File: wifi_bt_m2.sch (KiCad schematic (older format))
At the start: 24 parts, among them J1502 M.2_Key_E, Q1501 FDV301N, Q1502 FDV301N, SW1501 WWAN_HKS, U1502 74AUP2G00, U1504 NTB0104GU12, U1702 NTB0104GU12

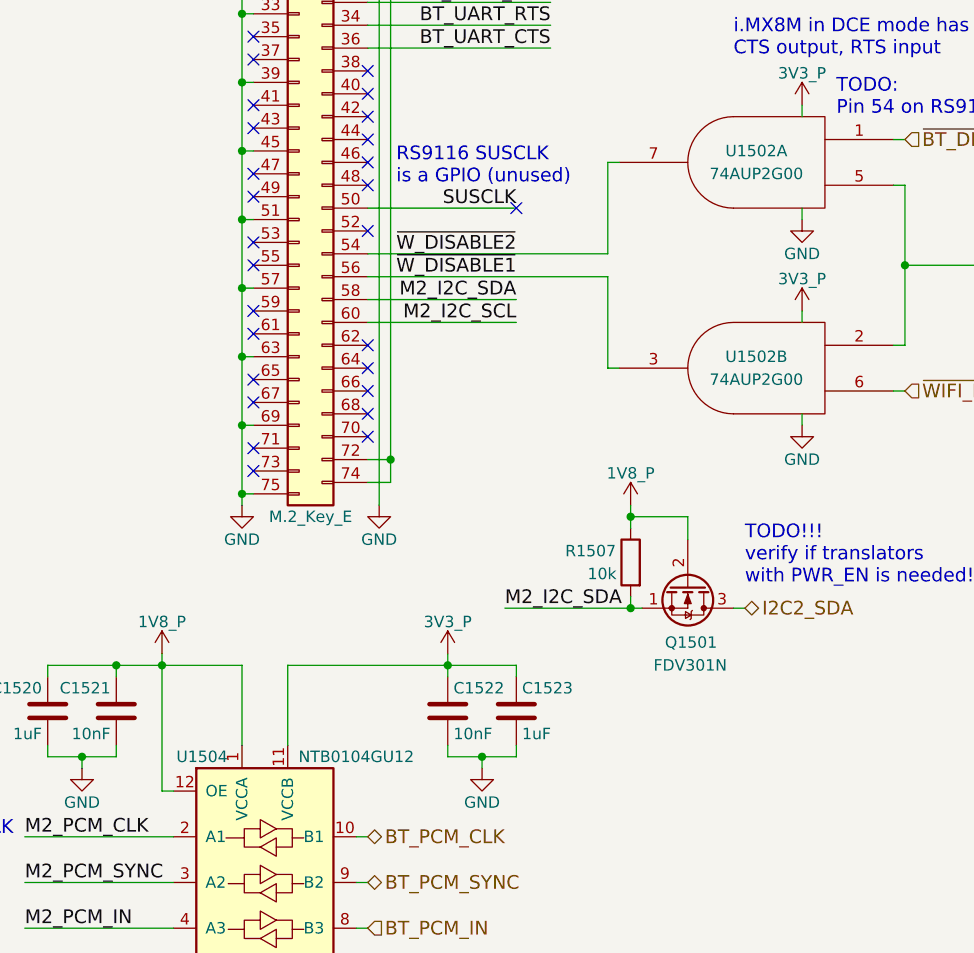
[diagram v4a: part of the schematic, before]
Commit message: Use SN74AUP2G08 instead of SN74AUP2G00 since the *08 is AND whereas the *00 is N AND
Since pin 54 is actually USB_VBUS sink on the RedPine module the baseboard may need to treat this pin specially (NXP EVK uses a NMOS inverter with a 10k pull-up to 3V3).
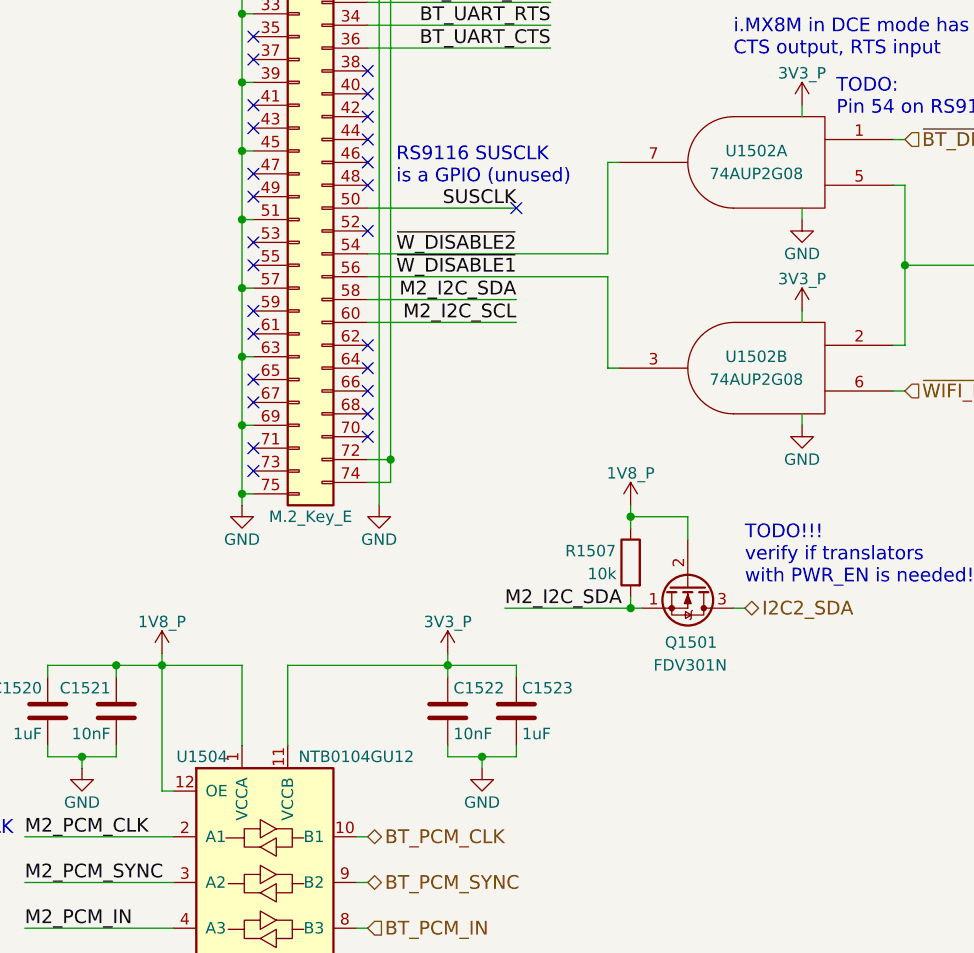
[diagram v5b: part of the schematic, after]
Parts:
- U1502: value 74AUP2G00 -> 74AUP2G08; Distrib Link https://www.digikey.com/product-detail/en/texas-instruments/SN74AUP2G00DCUR/296-36884-1-ND/4376315 -> https://www.digikey.com/product-detail/en/texas-instruments/SN74AUP2G08DCUR/296-32271-1-ND/3505517; Distrib PN 296-36884-1-ND -> 296-32271-1-ND; MFG Part Num SN74AUP2G00DCUR -> SN74AUP2G08DCUR; Others https://www.digikey.com/products/en/integrated-circuits-ics/logic-gates-and-inverters/705?quantity=&ColumnSort=1000011&page=1&k=74AUP2G00&pageSize=500 -> https://www.digikey.com/products/en/integrated-circuits-ics/logic-gates-and-inverters/705?k=74AUP2G08
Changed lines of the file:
@@
 P 7550 3550
 F 0 "U1502" H 7550 3600 50  0000 C CNN
-F 1 "74AUP2G00" H 7550 3500 50  0000 C CNN
+F 1 "74AUP2G08" H 7550 3500 50  0000 C CNN
 F 2 "" H 7550 3550 50  0001 C CNN
-F 3 "http://www.ti.com/lit/ds/symlink/sn74aup2g00.pdf" H 7550 3550 50  0001 C CNN
+F 3 "http://www.ti.com/lit/ds/symlink/sn74aup2g08.pdf" H 7550 3550 50  0001 C CNN
 F 4 "Texas Instruments" H 7550 3550 60  0001 C CNN "MFG Name"
-F 5 "SN74AUP2G00DCUR" H 7550 3550 60  0001 C CNN "MFG Part Num"
-F 6 "296-36884-1-ND" H 7550 3550 60  0001 C CNN "Distrib PN"
-F 7 "https://www.digikey.com/product-detail/en/texas-instruments/SN74AUP2G00DCUR/296-36884-1-ND/4376315" H 7550 3550 60  0001 C CNN "Distrib Link"
+F 5 "SN74AUP2G08DCUR" H 7550 3550 60  0001 C CNN "MFG Part Num"
+F 6 "296-32271-1-ND" H 7550 3550 60  0001 C CNN "Distrib PN"
+F 7 "https://www.digikey.com/product-detail/en/texas-instruments/SN74AUP2G08DCUR/296-32271-1-ND/3505517" H 7550 3550 60  0001 C CNN "Distrib Link"
 F 8 "-" H 7550 3550 60  0001 C CNN "Tolerance"
-F 9 "https://www.digikey.com/products/en/integrated-circuits-ics/logic-gates-and-inverters/705?quantity=&ColumnSort=1000011&page=1&k=74AUP2G00&pageSize=500" H 7550 3550 60  0001 C CNN "Others"
+F 9 "https://www.digikey.com/products/en/integrated-circuits-ics/logic-gates-and-inverters/705?k=74AUP2G08" H 7550 3550 60  0001 C CNN "Others"
 	1    7550 3550
 	-1   0    0    -1
@@
 	9650 5100 9400 5100
 Connection ~ 9400 5100
-$Comp
-L 74AUP2G00 U1502
-U 2 1 5AEC3CE9
-P 7550 4450
-F 0 "U1502" H 7550 4500 50  0000 C CNN
-F 1 "74AUP2G00" H 7550 4400 50  0000 C CNN
-F 2 "" H 7550 4450 50  0001 C CNN
-F 3 "http://www.ti.com/lit/ds/symlink/sn74aup2g00.pdf" H 7550 4450 50  0001 C CNN
-F 4 "Texas Instruments" H 7550 4450 60  0001 C CNN "MFG Name"
-F 5 "SN74AUP2G00DCUR" H 7550 4450 60  0001 C CNN "MFG Part Num"
-F 6 "296-36884-1-ND" H 7550 4450 60  0001 C CNN "Distrib PN"
-F 7 "https://www.digikey.com/product-detail/en/texas-instruments/SN74AUP2G00DCUR/296-36884-1-ND/4376315" H 7550 4450 60  0001 C CNN "Distrib Link"
-F 8 "-" H 7550 4450 60  0001 C CNN "Tolerance"
-F 9 "https://www.digikey.com/products/en/integrated-circuits-ics/logic-gates-and-inverters/705?quantity=&ColumnSort=1000011&page=1&k=74AUP2G00&pageSize=500" H 7550 4450 60  0001 C CNN "Others"
-	2    7550 4450
-	-1   0    0    -1
-$EndComp
 Text Notes 1150 7550 0    60   ~ 0
 internal 10k pull-up
@@
 	5400 7550 5400 7500
 Wire Wire Line
-	5000 6300 4950 6300
+	4950 6300 5000 6300
 Connection ~ 4950 5750
 Wire Wire Line
@@
 	5300 5750 5300 6100
 Wire Wire Line
-	4950 6300 4950 5700
+	4950 5700 4950 6300
 Wire Wire Line
 	1800 5700 1800 6300
@@
 Text Notes 2950 1250 0    60   ~ 0
 RS9116 datasheet says\nno WIFI_WAKE\nbut the schematic has it
+$Comp
+L 74AUP2G00 U1502
+U 2 1 5B14C873
+P 7550 4450
+F 0 "U1502" H 7550 4500 50  0000 C CNN
+F 1 "74AUP2G08" H 7550 4400 50  0000 C CNN
+F 2 "" H 7550 4450 50  0001 C CNN
+F 3 "http://www.ti.com/lit/ds/symlink/sn74aup2g08.pdf" H 7550 4450 50  0001 C CNN
+F 4 "Texas Instruments" H 7550 4450 60  0001 C CNN "MFG Name"
+F 5 "SN74AUP2G08DCUR" H 7550 4450 60  0001 C CNN "MFG Part Num"
+F 6 "296-32271-1-ND" H 7550 4450 60  0001 C CNN "Distrib PN"
+F 7 "https://www.digikey.com/product-detail/en/texas-instruments/SN74AUP2G08DCUR/296-32271-1-ND/3505517" H 7550 4450 60  0001 C CNN "Distrib Link"
+F 8 "-" H 7550 4450 60  0001 C CNN "Tolerance"
+F 9 "https://www.digikey.com/products/en/integrated-circuits-ics/logic-gates-and-inverters/705?k=74AUP2G08" H 7550 4450 60  0001 C CNN "Others"
+	2    7550 4450
+	-1   0    0    -1
+$EndComp
 $EndSCHEMATC

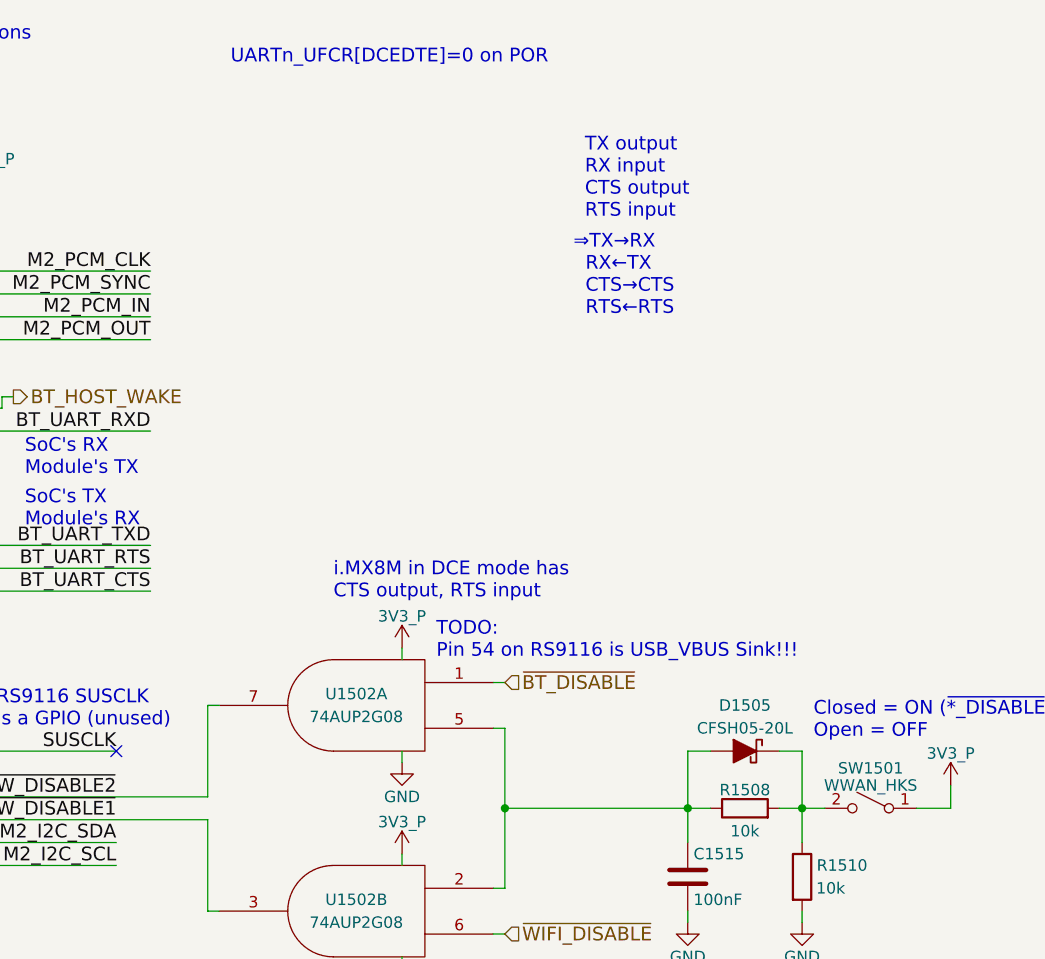
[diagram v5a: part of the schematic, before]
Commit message: Assign SAI5 to the WLAN/BT M.2, remove SIM2 slot due to conflicts between modules (specifically the L830-EB being a Config_0 module where the TX_BLANKING signal would connected to USIM_PWR2 sink), reassign the corresponding M.2 config pin to handle HP_DET, remove the AMOLED buck-boost as a different regulator will be used
The MIC_SEL, PROX_~INT, IMU_INT, and HAPTIC signals still need assigning
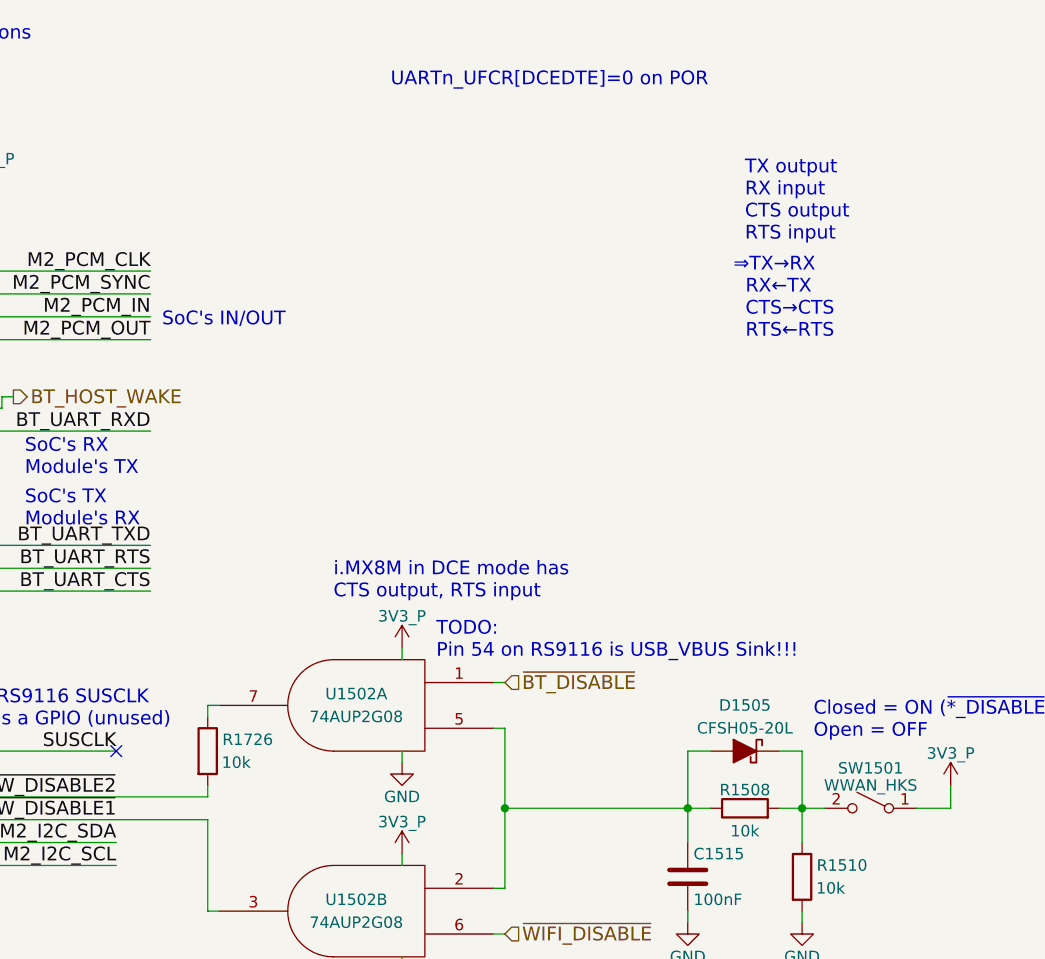
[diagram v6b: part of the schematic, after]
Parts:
- added R1726: 10k, symbol R
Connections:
- net ~W_DISABLE2: now also R1726.2; no longer U1502.7
- new net: R1726.1, U1502.7
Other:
- note added: "SoC's IN/OUT"
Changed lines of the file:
@@
 	5350 1500 5250 1500
 $Comp
-L GND #PWR0283
+L GND #PWR0256
 U 1 1 5B01D9F9
 P 5300 5050
-F 0 "#PWR0283" H 5300 4800 50  0001 C CNN
+F 0 "#PWR0256" H 5300 4800 50  0001 C CNN
 F 1 "GND" H 5300 4900 50  0000 C CNN
 F 2 "" H 5300 5050 50  0001 C CNN
@@
 Connection ~ 5300 5000
 $Comp
-L GND #PWR0284
+L GND #PWR0257
 U 1 1 5B01E5BE
 P 5900 5050
-F 0 "#PWR0284" H 5900 4800 50  0001 C CNN
+F 0 "#PWR0257" H 5900 4800 50  0001 C CNN
 F 1 "GND" H 5900 4900 50  0000 C CNN
 F 2 "" H 5900 5050 50  0001 C CNN
@@
 	5900 2150 5900 5050
 $Comp
-L 3V3_P #PWR0285
+L 3V3_P #PWR0258
 U 1 1 5B01E6B8
 P 5950 1300
-F 0 "#PWR0285" H 5950 1150 50  0001 C CNN
+F 0 "#PWR0258" H 5950 1150 50  0001 C CNN
 F 1 "3V3_P" H 5950 1440 50  0000 C CNN
 F 2 "" H 5950 1300 50  0001 C CNN
@@
 6.2 M.2 Signal Directions
 $Bitmap
-Pos 7850 1200
+Pos 8550 1300
 Scale 1.000000
 Data
@@
 EndData
 $EndBitmap
-Text Notes 8550 1425 0    60   ~ 0
+Text Notes 9250 1525 0    60   ~ 0
 TX output\nRX input\nCTS output\nRTS input
-Text Notes 8500 1850 0    60   ~ 0
+Text Notes 9200 1950 0    60   ~ 0
 ⇒TX→RX\n  RX←TX\n  CTS→CTS\n  RTS←RTS
 Text Notes 7450 3090 0    60   ~ 0
 i.MX8M in DCE mode has\nCTS output, RTS input
-Text Notes 7000 750  0    60   ~ 0
+Text Notes 7700 850  0    60   ~ 0
 UARTn_UFCR[DCEDTE]=0 on POR
 Wire Wire Line
@@
 $EndComp
 $Comp
-L 3V3_P #PWR0286
+L 3V3_P #PWR0259
 U 1 1 5B0C3C8A
 P 10150 3900
-F 0 "#PWR0286" H 10150 3750 50  0001 C CNN
+F 0 "#PWR0259" H 10150 3750 50  0001 C CNN
 F 1 "3V3_P" H 10150 4040 50  0000 C CNN
 F 2 "" H 10150 3900 50  0001 C CNN
@@
 Wire Wire Line
 	6900 4450 6950 4450
-Wire Wire Line
-	6900 3950 6900 3550
 Wire Wire Line
 	6900 3550 6950 3550
@@
 NoConn ~ 6500 3750
 $Comp
-L 3V3_P #PWR0287
+L 3V3_P #PWR0260
 U 1 1 5B0D90EE
 P 7750 3300
-F 0 "#PWR0287" H 7750 3150 50  0001 C CNN
+F 0 "#PWR0260" H 7750 3150 50  0001 C CNN
 F 1 "3V3_P" H 7750 3440 50  0000 C CNN
 F 2 "" H 7750 3300 50  0001 C CNN
@@
 	7750 3300 7750 3350
 $Comp
-L GND #PWR0288
+L GND #PWR0261
 U 1 1 5B0D91C5
 P 7750 4700
-F 0 "#PWR0288" H 7750 4450 50  0001 C CNN
+F 0 "#PWR0261" H 7750 4450 50  0001 C CNN
 F 1 "GND" H 7750 4550 50  0000 C CNN
 F 2 "" H 7750 4700 50  0001 C CNN
@@
 Connection ~ 4550 2400
 $Comp
-L 1V8_P #PWR0289
+L 1V8_P #PWR0262
 U 1 1 5AEFAF82
 P 4550 2000
-F 0 "#PWR0289" H 4550 1850 50  0001 C CNN
+F 0 "#PWR0262" H 4550 1850 50  0001 C CNN
 F 1 "1V8_P" H 4550 2140 50  0000 C CNN
 F 2 "" H 4550 2000 50  0001 C CNN
@@
 $EndComp
 $Comp
-L 1V8_P #PWR0290
+L 1V8_P #PWR0263
 U 1 1 5AEB9155
 P 7000 5050
-F 0 "#PWR0290" H 7000 4900 50  0001 C CNN
+F 0 "#PWR0263" H 7000 4900 50  0001 C CNN
 F 1 "1V8_P" H 7000 5190 50  0000 C CNN
 F 2 "" H 7000 5050 50  0001 C CNN
@@
 TODO!!!\nverify if translators\nwith PWR_EN is needed!
 $Comp
-L 3V3_P #PWR0291
+L 3V3_P #PWR0264
 U 1 1 5AF2CD0D
 P 7750 4200
-F 0 "#PWR0291" H 7750 4050 50  0001 C CNN
+F 0 "#PWR0264" H 7750 4050 50  0001 C CNN
 F 1 "3V3_P" H 7750 4340 50  0000 C CNN
 F 2 "" H 7750 4200 50  0001 C CNN
@@
 	7750 4200 7750 4250
 $Comp
-L GND #PWR0292
+L GND #PWR0265
 U 1 1 5AF2CDB4
 P 7750 3800
-F 0 "#PWR0292" H 7750 3550 50  0001 C CNN
+F 0 "#PWR0265" H 7750 3550 50  0001 C CNN
 F 1 "GND" H 7750 3650 50  0000 C CNN
 F 2 "" H 7750 3800 50  0001 C CNN
@@
 $EndComp
 $Comp
-L GND #PWR0293
+L GND #PWR0266
 U 1 1 5AF3C984
 P 9000 4500
-F 0 "#PWR0293" H 9000 4250 50  0001 C CNN
+F 0 "#PWR0266" H 9000 4250 50  0001 C CNN
 F 1 "GND" H 9000 4350 50  0000 C CNN
 F 2 "" H 9000 4500 50  0001 C CNN
@@
 $EndComp
 $Comp
-L GND #PWR0294
+L GND #PWR0267
 U 1 1 5AF3C98A
 P 9500 4500
-F 0 "#PWR0294" H 9500 4250 50  0001 C CNN
+F 0 "#PWR0267" H 9500 4250 50  0001 C CNN
 F 1 "GND" H 9500 4350 50  0000 C CNN
 F 2 "" H 9500 4500 50  0001 C CNN
@@
 $EndComp
 $Comp
-L 1V8_P #PWR0295
+L 1V8_P #PWR0268
 U 1 1 5AEBC081
 P 9400 5050
-F 0 "#PWR0295" H 9400 4900 50  0001 C CNN
+F 0 "#PWR0268" H 9400 4900 50  0001 C CNN
 F 1 "1V8_P" H 9400 5190 50  0000 C CNN
 F 2 "" H 9400 5050 50  0001 C CNN
@@
 $EndComp
 $Comp
-L GND #PWR0296
+L GND #PWR0269
 U 1 1 5B2489BD
 P 6350 6200
-F 0 "#PWR0296" H 6350 5950 50  0001 C CNN
+F 0 "#PWR0269" H 6350 5950 50  0001 C CNN
 F 1 "GND" H 6350 6050 50  0000 C CNN
 F 2 "" H 6350 6200 50  0001 C CNN
@@
 $EndComp
 $Comp
-L GND #PWR0297
+L GND #PWR0270
 U 1 1 5B2489DB
 P 4600 6200
-F 0 "#PWR0297" H 4600 5950 50  0001 C CNN
+F 0 "#PWR0270" H 4600 5950 50  0001 C CNN
 F 1 "GND" H 4600 6050 50  0000 C CNN
 F 2 "" H 4600 6200 50  0001 C CNN
@@
 	4450 5750 5300 5750
 $Comp
-L GND #PWR0298
+L GND #PWR0271
 U 1 1 5B2489F2
 P 5400 7550
-F 0 "#PWR0298" H 5400 7300 50  0001 C CNN
+F 0 "#PWR0271" H 5400 7300 50  0001 C CNN
 F 1 "GND" H 5400 7400 50  0000 C CNN
 F 2 "" H 5400 7550 50  0001 C CNN
@@
 BCLK
 $Comp
-L 3V3_P #PWR0299
+L 3V3_P #PWR0272
 U 1 1 5B248A11
 P 6200 5700
-F 0 "#PWR0299" H 6200 5550 50  0001 C CNN
+F 0 "#PWR0272" H 6200 5550 50  0001 C CNN
 F 1 "3V3_P" H 6200 5840 50  0000 C CNN
 F 2 "" H 6200 5700 50  0001 C CNN
@@
 $EndComp
 $Comp
-L 1V8_P #PWR0300
+L 1V8_P #PWR0273
 U 1 1 5B248A1D
 P 4950 5700
-F 0 "#PWR0300" H 4950 5550 50  0001 C CNN
+F 0 "#PWR0273" H 4950 5550 50  0001 C CNN
 F 1 "1V8_P" H 4950 5840 50  0000 C CNN
 F 2 "" H 4950 5700 50  0001 C CNN
@@
 $EndComp
 $Comp
-L GND #PWR0301
+L GND #PWR0274
 U 1 1 5B337EDE
 P 3200 6200
-F 0 "#PWR0301" H 3200 5950 50  0001 C CNN
+F 0 "#PWR0274" H 3200 5950 50  0001 C CNN
 F 1 "GND" H 3200 6050 50  0000 C CNN
 F 2 "" H 3200 6200 50  0001 C CNN
@@
 $EndComp
 $Comp
-L GND #PWR0302
+L GND #PWR0275
 U 1 1 5B337EFC
 P 1450 6200
-F 0 "#PWR0302" H 1450 5950 50  0001 C CNN
+F 0 "#PWR0275" H 1450 5950 50  0001 C CNN
 F 1 "GND" H 1450 6050 50  0000 C CNN
 F 2 "" H 1450 6200 50  0001 C CNN
@@
 	1300 5750 2150 5750
 $Comp
-L GND #PWR0303
+L GND #PWR0276
 U 1 1 5B337F13
 P 2250 7550
-F 0 "#PWR0303" H 2250 7300 50  0001 C CNN
+F 0 "#PWR0276" H 2250 7300 50  0001 C CNN
 F 1 "GND" H 2250 7400 50  0000 C CNN
 F 2 "" H 2250 7550 50  0001 C CNN
@@
 	2650 7100 2700 7100
 $Comp
-L 3V3_P #PWR0304
+L 3V3_P #PWR0277
 U 1 1 5B337F23
 P 3050 5700
-F 0 "#PWR0304" H 3050 5550 50  0001 C CNN
+F 0 "#PWR0277" H 3050 5550 50  0001 C CNN
 F 1 "3V3_P" H 3050 5840 50  0000 C CNN
 F 2 "" H 3050 5700 50  0001 C CNN
@@
 $EndComp
 $Comp
-L 1V8_P #PWR0305
+L 1V8_P #PWR0278
 U 1 1 5B337F29
 P 1800 5700
-F 0 "#PWR0305" H 1800 5550 50  0001 C CNN
+F 0 "#PWR0278" H 1800 5550 50  0001 C CNN
 F 1 "1V8_P" H 1800 5840 50  0000 C CNN
 F 2 "" H 1800 5700 50  0001 C CNN
@@
 	-1   0    0    -1
 $EndComp
+Text Notes 6700 1900 0    60   ~ 0
+SoC's IN/OUT
+$Comp
+L R R1726
+U 1 1 5B29F993
+P 6900 3750
+F 0 "R1726" H 7075 3800 50  0000 C CNN
+F 1 "10k" H 7025 3700 50  0000 C CNN
+F 2 "" V 6830 3750 50  0001 C CNN
+F 3 "" H 6900 3750 50  0001 C CNN
+	1    6900 3750
+	1    0    0    -1
+$EndComp
+Wire Wire Line
+	6900 3600 6900 3550
+Wire Wire Line
+	6900 3950 6900 3900
 $EndSCHEMATC
